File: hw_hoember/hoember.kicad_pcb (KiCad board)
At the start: 2 copper layers, 27.9 x 55 mm, 42 parts, among them J1 Conn_2Rows-05Pins, Q1 AO3401A, Q2 AO3401A, Q3 AO3401A, SW1 SW_DPST_x2, T1 Tab, U1 PY32F002AF15P6TU

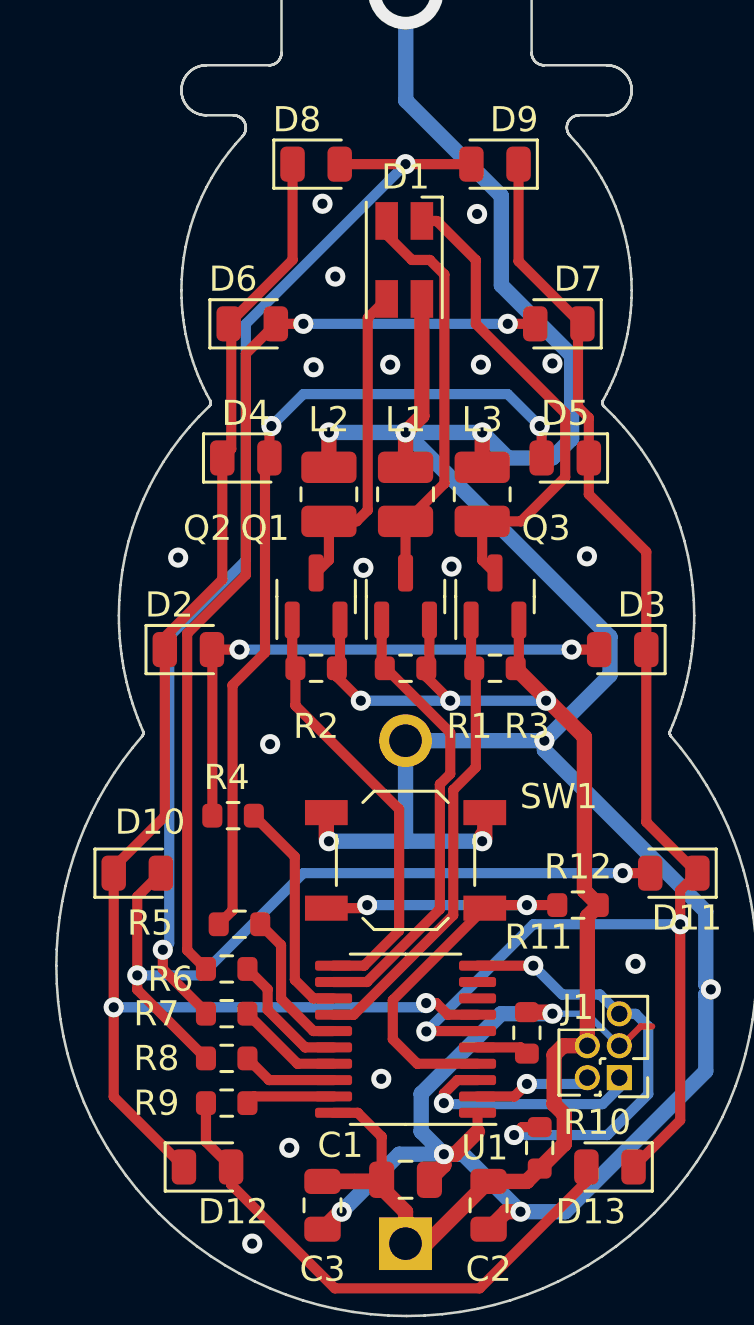
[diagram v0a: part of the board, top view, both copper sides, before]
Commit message: Added hoember and mezi panel
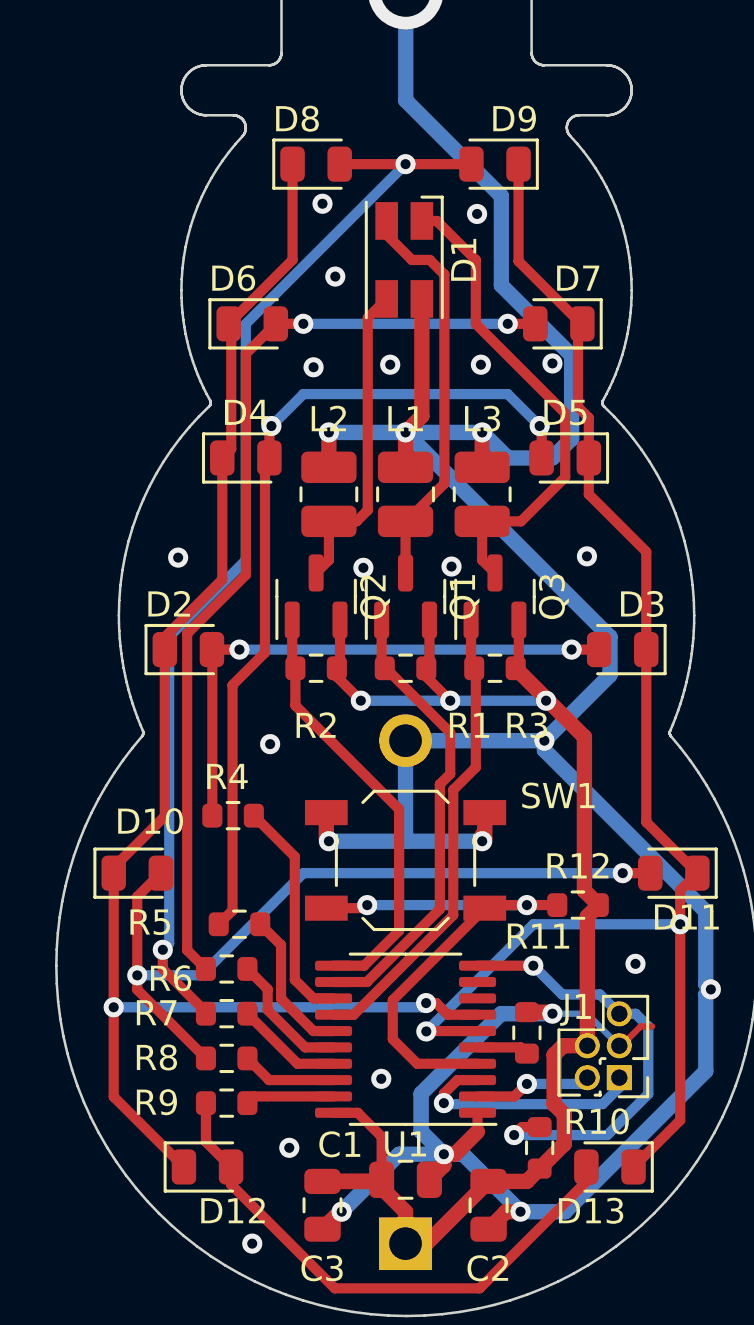
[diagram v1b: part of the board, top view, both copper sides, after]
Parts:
- added T1: Tab, kikit:Tab, F.Cu at (113.3, 84.8)
- added T1: Tab, kikit:Tab, F.Cu at (147.1, 84.8)
- D1: footprint LED_SMD:LED_RGB_Wuerth-PLCC4_3.2x2.8mm_150141M173100 -> karifa:LED_RGB_Wuerth-PLCC4_3.2x2.8mm_150141M173100
- Q1, Q2, Q3: footprint sajat:SOT-23 -> karifa:SOT-23
- U1: footprint Package_SO:TSSOP-20_4.4x6.5mm_P0.65mm -> karifa:TSSOP-20_4.4x6.5mm_P0.65mm
- moved T1 16.5 mm to (118.9, 56.6)
- moved T1 15.7 mm to (142.5, 56.6)
- turned D1 to 90 degrees
- turned U1 to 0 degrees
